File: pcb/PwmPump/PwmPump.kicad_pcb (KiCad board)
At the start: 2 copper layers, 50 x 38 mm, 7 parts, among them J1 3.5mm, J2 3.5mm, U1 WEMOS_C3_mini, U2 BOB-12009

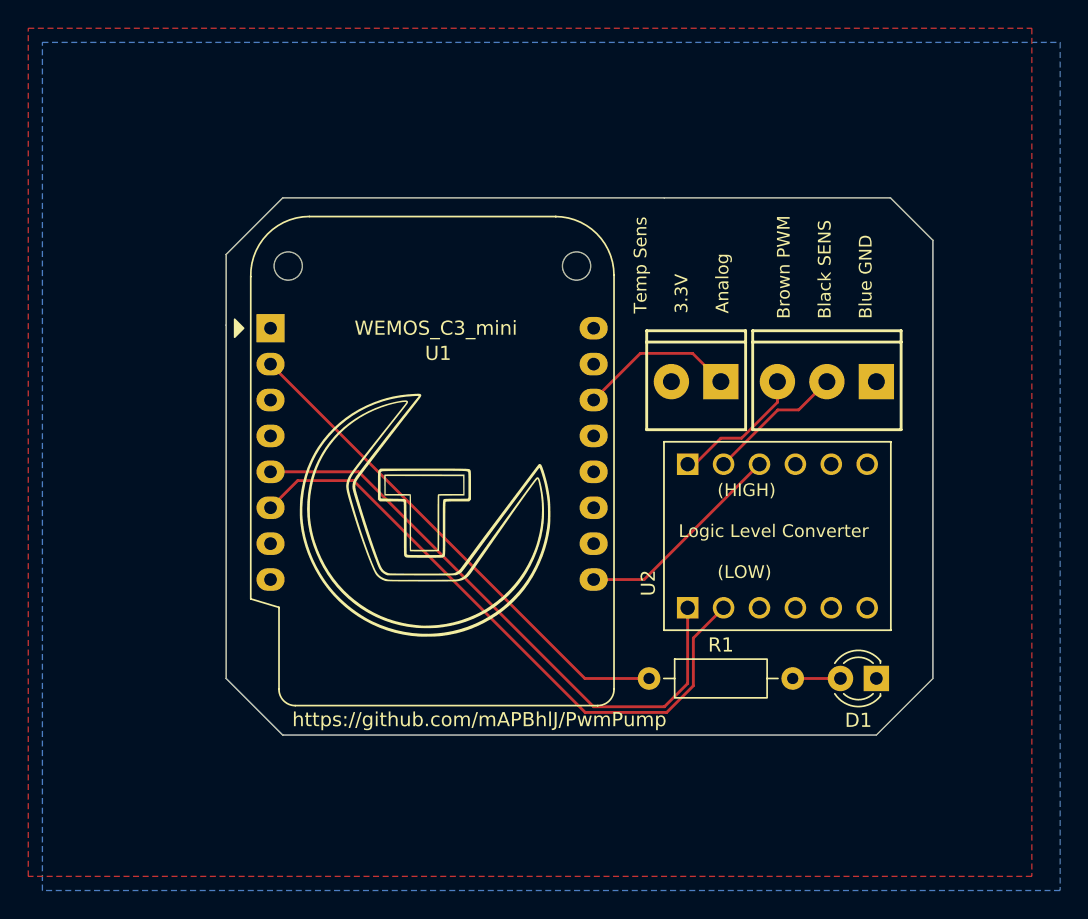
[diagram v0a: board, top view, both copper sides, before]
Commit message: Updated: Added 2nd analog input
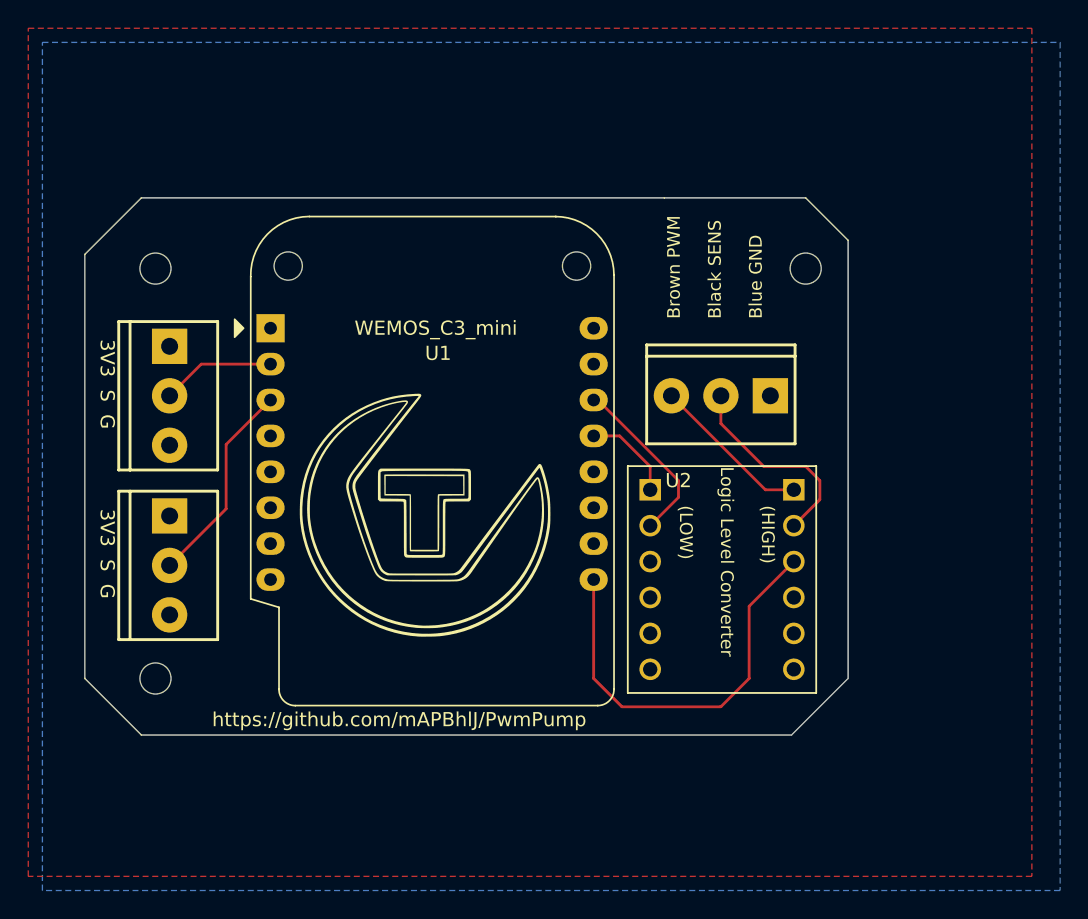
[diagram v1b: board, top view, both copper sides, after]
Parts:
- removed D1: LED, LED_THT:LED_D3.0mm
- removed R1: 220, Resistor_THT:R_Axial_DIN0207_L6.3mm_D2.5mm_P10.16mm_Horizontal
- added J3: 3.5mm, PCM_SparkFun-Connector:ScrewTerminal_1x03_P3.5mm_Horizontal_Black, F.Cu at (59.0, 82.5)
- added REF**: MountingHole_2.2mm_M2_DIN965, MountingHole:MountingHole_2.2mm_M2_DIN965, F.Cu at (58.0, 106.0)
- added REF**: MountingHole_2.2mm_M2_DIN965, MountingHole:MountingHole_2.2mm_M2_DIN965, F.Cu at (104.0, 77.0)
- added REF**: MountingHole_2.2mm_M2_DIN965, MountingHole:MountingHole_2.2mm_M2_DIN965, F.Cu at (58.0, 77.0)
- J2: footprint PCM_SparkFun-Connector:ScrewTerminal_1x02_P3.5mm_Horizontal_Black -> PCM_SparkFun-Connector:ScrewTerminal_1x03_P3.5mm_Horizontal_Black
- moved J2 40.1 mm to (59.0, 94.5), turned to -90 degrees
- moved J1 7.57 mm to (101.5, 86.0)
- moved U2 4.99 mm to (98.1, 99.0), turned to 0 degrees
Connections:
- J2 pad 1: Net-(J2-Pin_1) -> +3.3V
- J2 pad 2: +3.3V -> Net-(J2-Pin_2)
- U1 pad 11: EC11_A -> unconnected-(U1-D6-Pad11)
- U1 pad 12: EC11_BTN -> unconnected-(U1-D7-Pad12)
- U1 pad 13: unconnected-(U1-D8-Pad13) -> Net-(U1-D8)
- U1 pad 14: Net-(J2-Pin_1) -> Net-(U1-D10)
- U1 pad 3: OLED_SDA -> Net-(J2-Pin_2)
- U1 pad 4: OLED_SCL -> unconnected-(U1-D1-Pad4)
- U1 pad 5: Net-(U1-D0) -> unconnected-(U1-D0-Pad5)
- U1 pad 6: Net-(U1-D4) -> unconnected-(U1-D4-Pad6)
- U1 pad 7: EC11_B -> unconnected-(U1-D5-Pad7)
- U2 pad LV1: Net-(U1-D0) -> Net-(U1-D8)
- U2 pad LV2: Net-(U1-D4) -> Net-(U1-D10)
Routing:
- net Net-(U1-D4): track 44.7 -> 0.00 mm
- net Net-(U1-D0): track 42.4 -> 0.00 mm
- net Net-(J3-Pin_2): track 36.0 -> 8.07 mm
- net Net-(J2-Pin_2): track 0.00 -> 14.7 mm
- net +5V: track 15.1 -> 29.2 mm
- net Net-(U1-D10): track 0.00 -> 12.4 mm
- net Net-(J2-Pin_1): track 11.2 -> 0.00 mm
- net Net-(U1-D8): track 0.00 -> 6.54 mm
- net Net-(J1-Pin_2): track 9.73 -> 14.6 mm
- net Net-(D1-A): track 3.38 -> 0.00 mm
- net Net-(J1-Pin_3): track 9.63 -> 11.4 mm
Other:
- board size 50 x 38 mm -> 54 x 38 mm
- board text added: "3V3 S G"
- board text removed: "Temp Sens 3.3V Analog"
